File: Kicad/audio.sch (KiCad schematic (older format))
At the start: 70 parts, among them J201 CD Audio In, J202 AC'97 Audio Header, J203 Line Out, U201 TLV320AIC23BPW, U202 STX-4335-5BGP-S1, Y201 12M 20pF

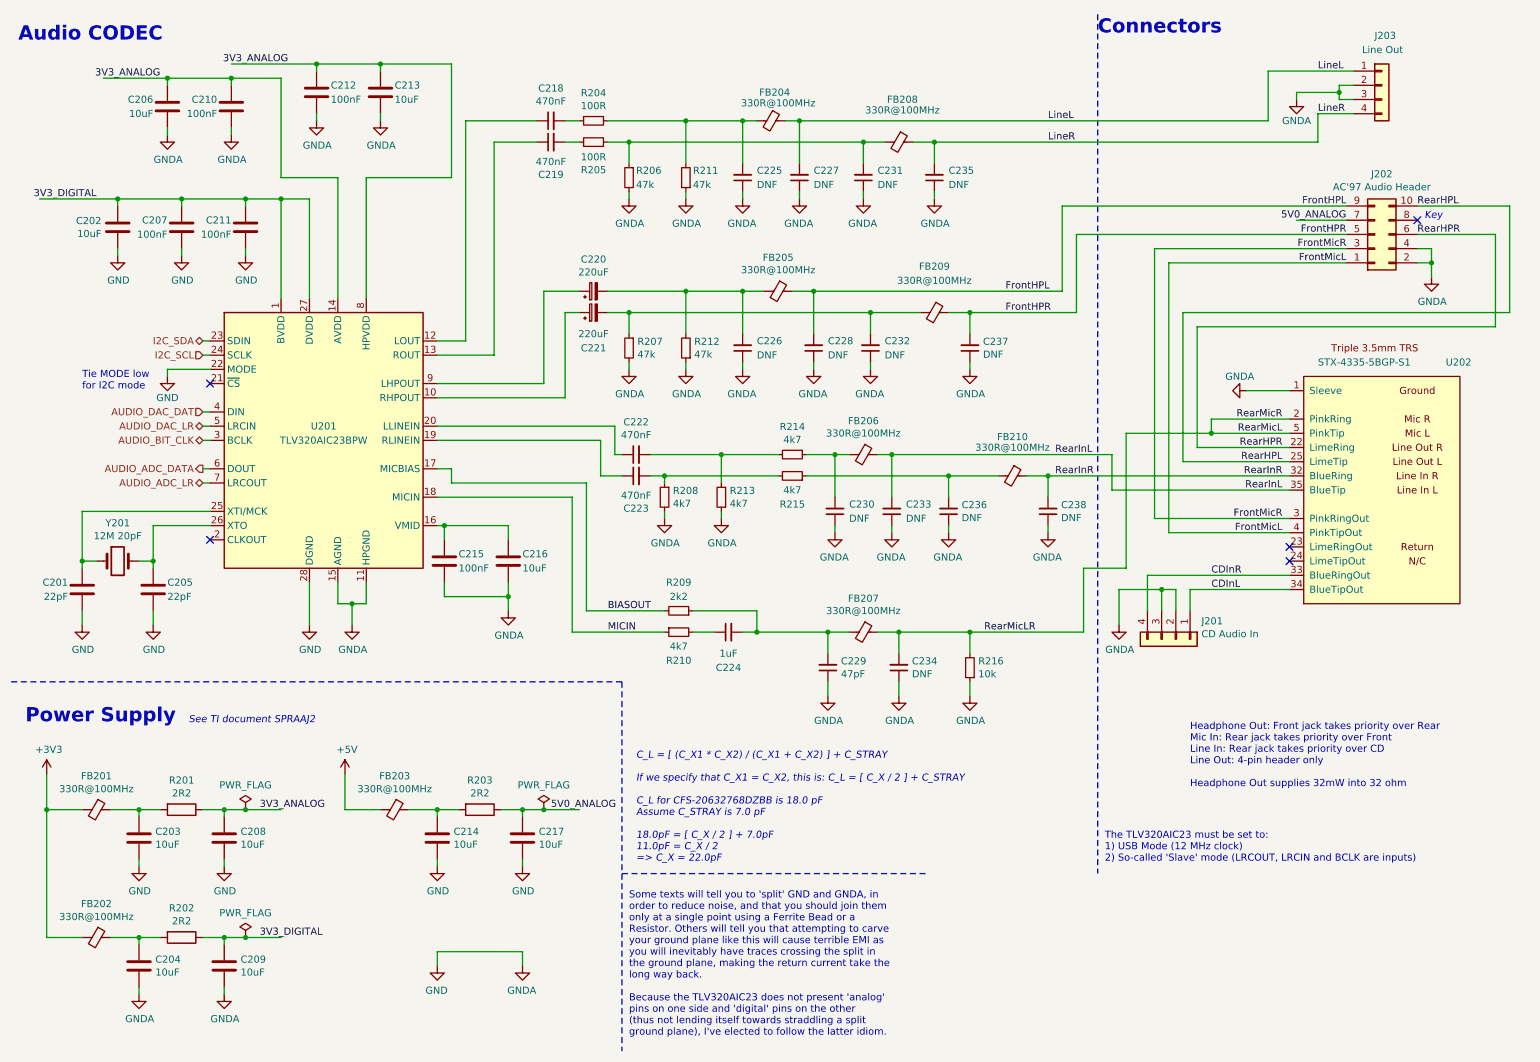
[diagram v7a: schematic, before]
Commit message: Added expansion header.
Involved rerouting quite a few things.
Also added through-hole switches for power/reset.
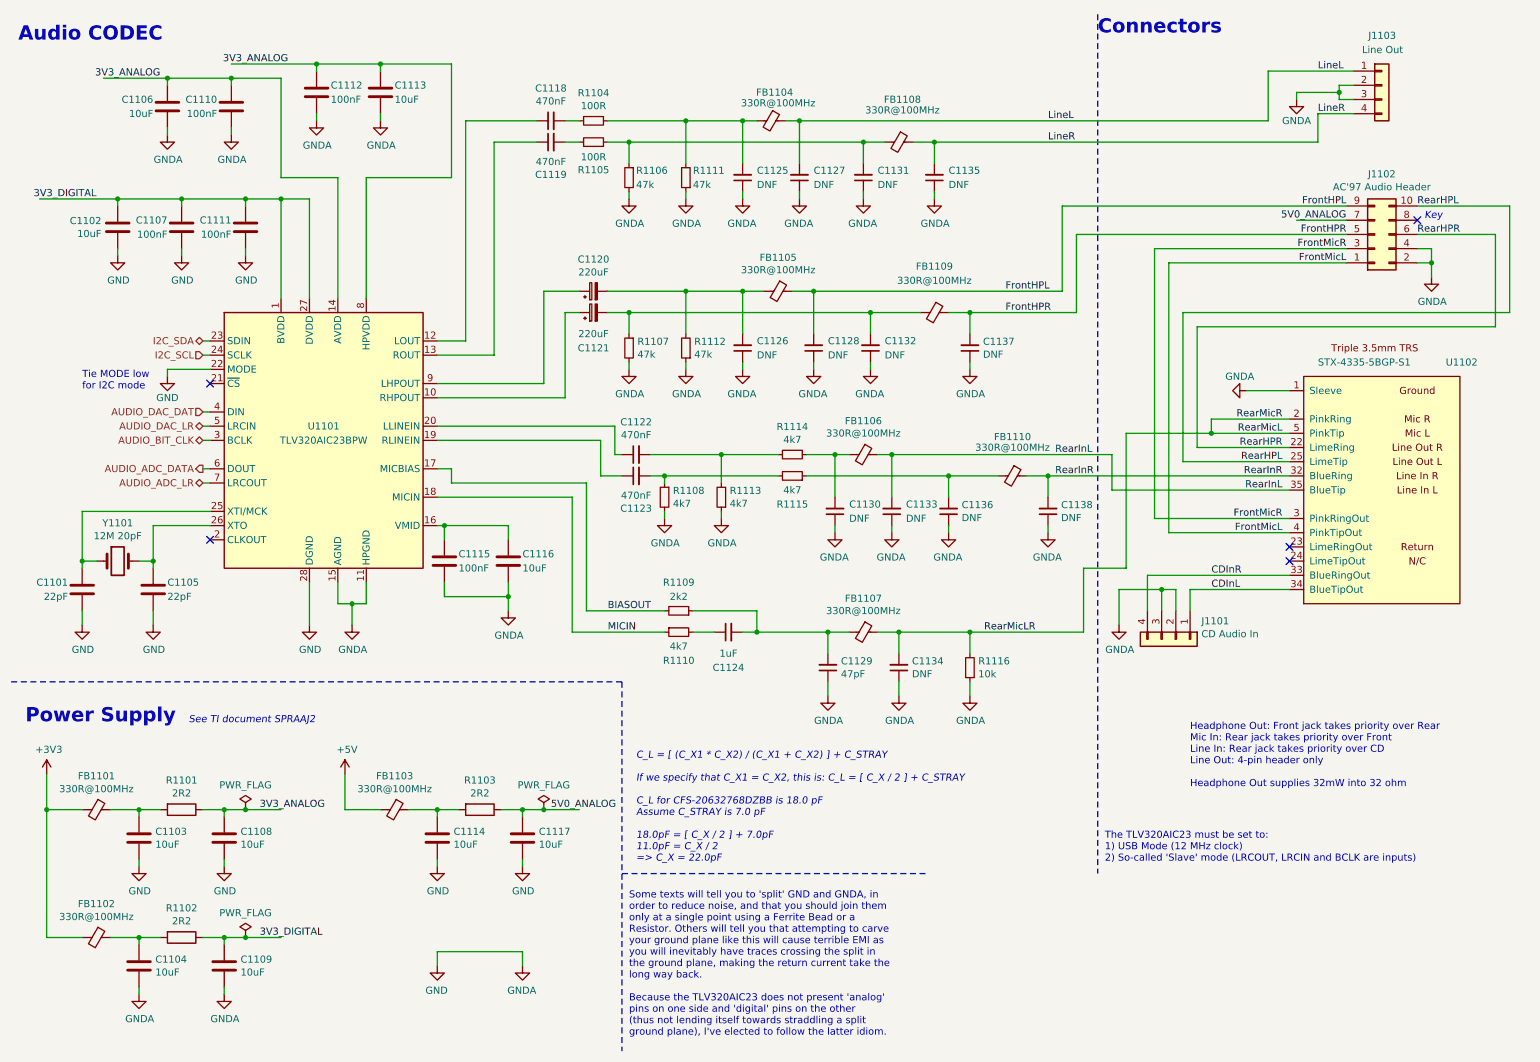
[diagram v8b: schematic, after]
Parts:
- renumbered C201 to C1101, C202 to C1102, C203 to C1103, C204 to C1104, C205 to C1105, C206 to C1106, C207 to C1107, C208 to C1108, C209 to C1109, C210 to C1110, C211 to C1111, C212 to C1112, C213 to C1113, C214 to C1114, C215 to C1115, C216 to C1116, C217 to C1117, C218 to C1118, C219 to C1119, C220 to C1120, C221 to C1121, C222 to C1122, C223 to C1123, C224 to C1124, C225 to C1125, C226 to C1126, C227 to C1127, C228 to C1128, C229 to C1129, C230 to C1130, C231 to C1131, C232 to C1132, C233 to C1133, C234 to C1134, C235 to C1135, C236 to C1136, C237 to C1137, C238 to C1138, FB201 to FB1101, FB202 to FB1102, FB203 to FB1103, FB204 to FB1104, FB205 to FB1105, FB206 to FB1106, FB207 to FB1107, FB208 to FB1108, FB209 to FB1109, FB210 to FB1110, J201 to J1101, J202 to J1102, J203 to J1103, R201 to R1101, R202 to R1102, R203 to R1103, R204 to R1104, R205 to R1105, R206 to R1106, R207 to R1107, R208 to R1108, R209 to R1109, R210 to R1110, R211 to R1111, R212 to R1112, R213 to R1113, R214 to R1114, R215 to R1115, R216 to R1116, U201 to U1101, U202 to U1102, Y201 to Y1101
